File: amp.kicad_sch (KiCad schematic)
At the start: 5 parts, among them T1 BN-43-202

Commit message: working on Amp.  Stuck on symbol for RD16HHF1
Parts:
- added C22, C24: 0.1, symbol Device:C
- added C23: 0.01, symbol Device:C
- added R11, R12: 470, symbol Device:R
- added RV1, RV2: 20K, symbol Device:R_Potentiometer
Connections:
- net GND: now also T1.2 (AB), C22.1, C24.1, RV1.1, RV2.1
- net K2-14: now also C21.2, R11.2
- net at T1.3 (SA): now also C23.1
- new net: C22.2, R11.1, RV1.2
- new net: C24.2, R12.2, RV2.2
- new net: C23.2, R12.1
- new net +5V REG: RV1.3, RV2.3

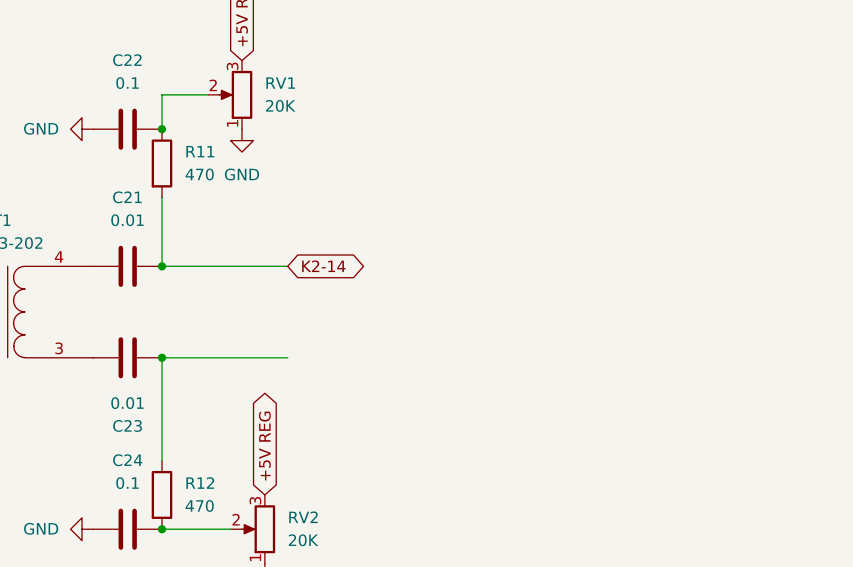
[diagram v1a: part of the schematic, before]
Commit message: modeled RD16HHF1 and added it to Amp.  ERC passes
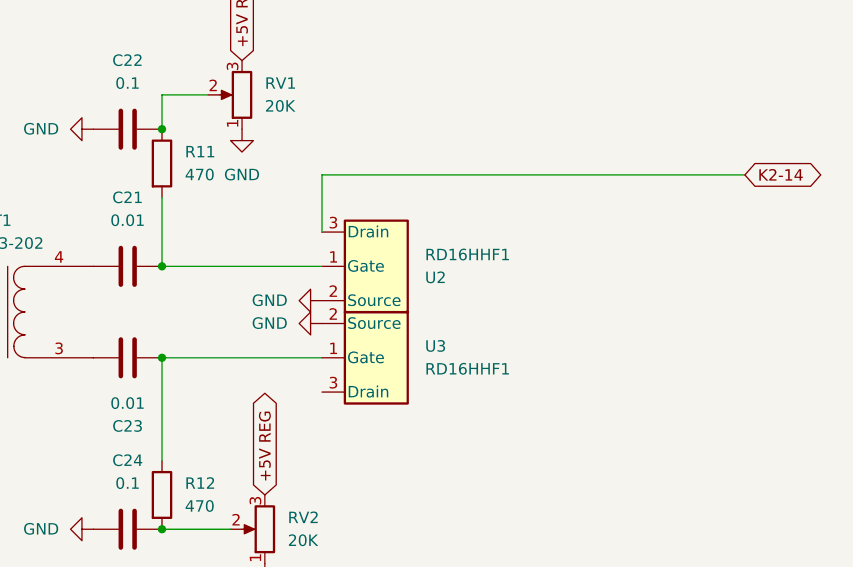
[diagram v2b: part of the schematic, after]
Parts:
- added U2, U3: RD16HHF1, Package_TO_SOT_THT:TO-220-3_Vertical, symbol ZZZMyLibrary:RD16HHF1
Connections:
- net GND: now also U2.2 (Source), U3.2 (Source)
- net K2-14: now also U2.3 (Drain); no longer C21.2, R11.2
- net at C23.2, R12.1: now also U3.1 (Gate)
- new net: C21.2, R11.2, U2.1 (Gate)

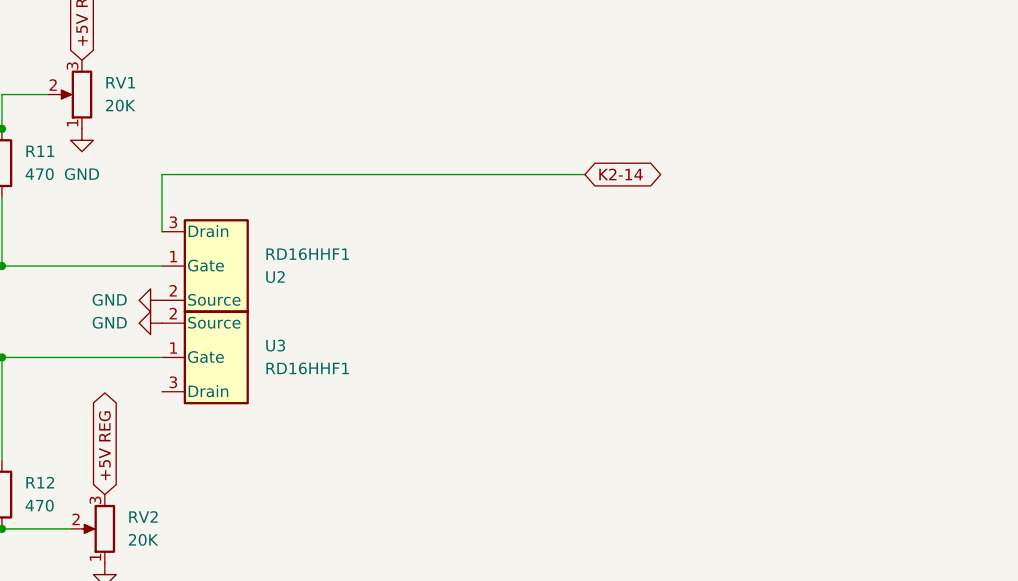
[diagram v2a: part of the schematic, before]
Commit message: first pass at amp ckt.  had to create a few parts, so these should be checked VERY carefully
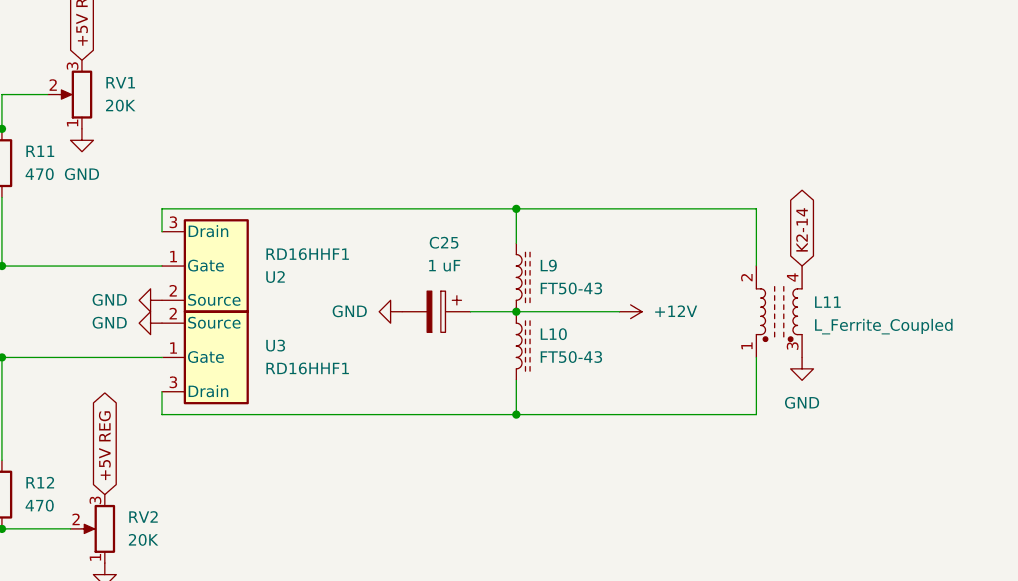
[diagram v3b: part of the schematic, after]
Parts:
- added C25: 1 uF, symbol Device:C_Polarized
- added L10, L9: FT50-43, symbol Device:L_Ferrite
- added L11: L_Ferrite_Coupled, symbol Device:L_Ferrite_Coupled
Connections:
- net GND: now also C25.2, L11.3
- net K2-14: now also L11.4; no longer U2.3 (Drain)
- net at U3.3 (Drain): now also L10.2, L11.1
- new net: L11.2, L9.1, U2.3 (Drain)
- new net +12V: C25.1, L10.1, L9.2
